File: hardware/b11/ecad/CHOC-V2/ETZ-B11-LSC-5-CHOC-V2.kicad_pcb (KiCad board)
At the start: 2 copper layers, 131.5 x 85.8 mm, 44 parts, among them SW1 Kailh_socket_PG1350, SW10 Kailh_socket_PG1350, SW11 Kailh_socket_PG1350, SW12 Kailh_socket_PG1350, SW13 Kailh_socket_PG1350, SW14 Kailh_socket_PG1350, SW15 Kailh_socket_PG1350, SW16 Kailh_socket_PG1350, SW17 Kailh_socket_PG1350, SW18 Kailh_socket_PG1350, SW19 Kailh_socket_PG1350, SW2 Kailh_socket_PG1350, SW20 Kailh_socket_PG1350, SW21 Kailh_socket_PG1350, SW22 Kailh_socket_PG1350, SW3 Kailh_socket_PG1350, SW4 Kailh_socket_PG1350, SW5 Kailh_socket_PG1350, SW6 Kailh_socket_PG1350, SW7 Kailh_socket_PG1350, SW8 Kailh_socket_PG1350, SW9 Kailh_socket_PG1350

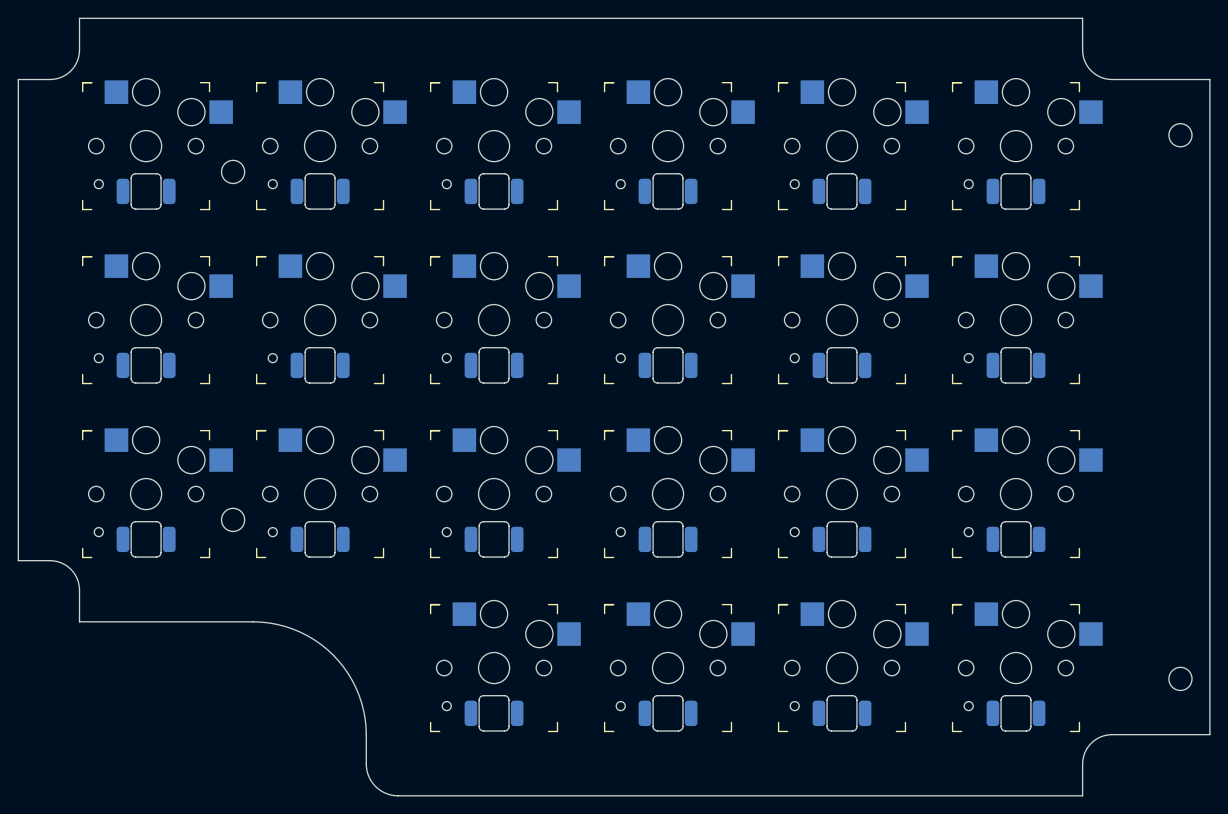
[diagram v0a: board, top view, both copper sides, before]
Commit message: refactor(hardware/b11): restructure ecad + tools, add KS-33 boards
- Rename PCB files: *-N → *-MX, *-L → *-CHOC-V2
- Reorganise ecad/ into per-family subfolders (MX/, CHOC-V2/, KS-33/)
- Add 8 blank KS-33 boards (outline only, human-populated ad-hoc)
- Apply JLCPCB-validated stackup (white/black/FR4 natural/black/white)
  to all 24 boards; SP boards at correct family thickness
- Add hardware/b11/tools/: config.py, placement.py, place-switch-sockets.py,
  place-switch-leds.py, place-display-leds.py — family-aware, non-destructive
- Archive old placement + generation scripts to hardware/scripts/_archive/
- Remove switch-origins.yaml (replaced by GRID_ORIGINS in config.py)
- Add PLAN.md tracking refactor progress

Co-Authored-By: Claude Sonnet 4.6 <noreply@anthropic.com>
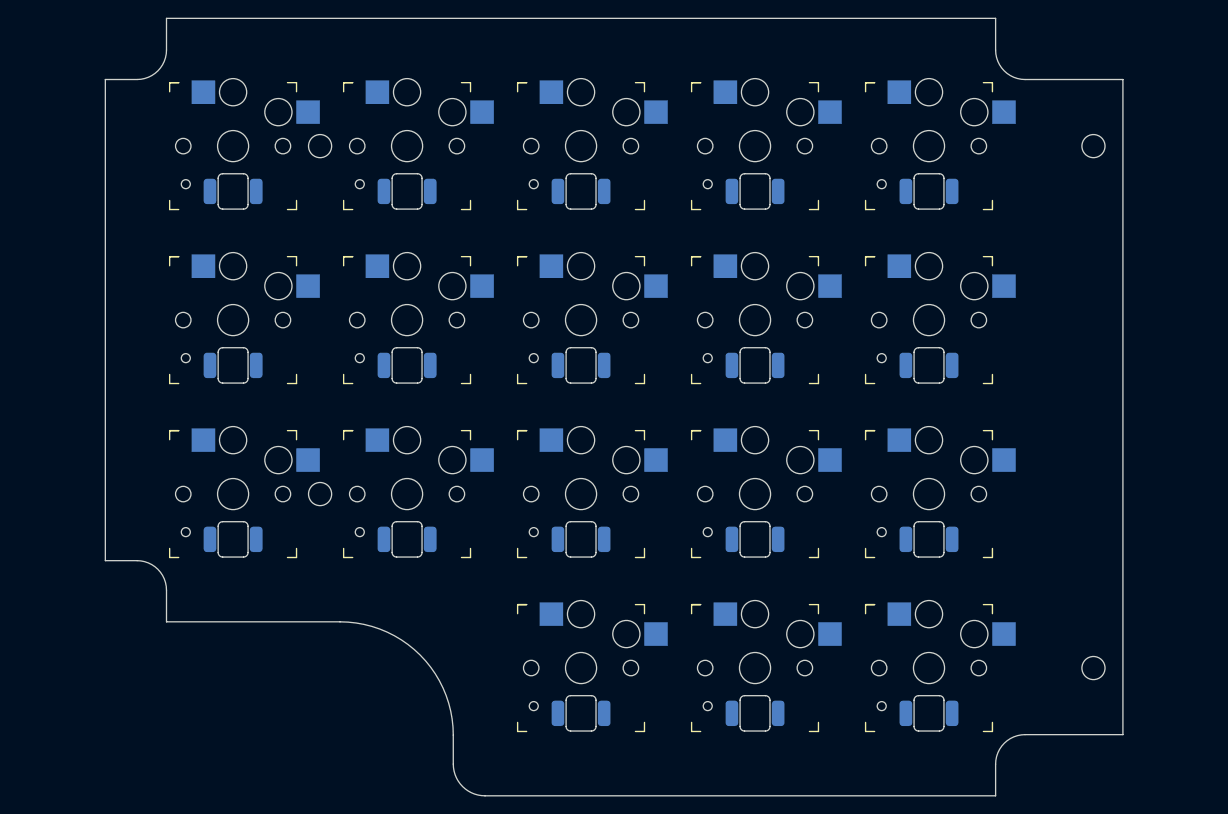
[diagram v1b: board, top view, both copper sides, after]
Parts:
- removed LED19, LED20, LED21, LED22: LED_SMD_6028_BackMount, LED_SMD_6028_BackMount
- removed SW19, SW20, SW21, SW22: Kailh_socket_PG1350, Kailh_socket_PG1350
- moved LED6 88.5 mm to (106.4, 97.5)
- moved SW6 88.5 mm to (106.4, 92.5)
- moved LED12 69.9 mm to (125.6, 116.7)
- moved SW12 69.9 mm to (125.6, 111.7)
- moved LED11 69.9 mm to (106.4, 116.7)
- moved SW11 69.9 mm to (106.4, 111.7)
- moved LED14 48.0 mm to (164.0, 116.7)
- moved SW14 48.0 mm to (164.0, 111.7)
- moved LED13 48.0 mm to (144.8, 116.7)
- moved LED15 48.0 mm to (183.2, 116.7)
- moved SW13 48.0 mm to (144.8, 111.7)
- moved SW15 48.0 mm to (183.2, 111.7)
- moved LED10 28.8 mm to (183.2, 97.5)
- moved LED9 28.8 mm to (164.0, 97.5)
- moved SW10 28.8 mm to (183.2, 92.5)
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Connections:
- SW10 pad 2: COL3 -> COL4
- SW11 pad 1: ROW1 -> ROW2
- SW11 pad 2: COL4 -> COL0
- SW12 pad 1: ROW1 -> ROW2
- SW12 pad 2: COL5 -> COL1
- SW13 pad 2: COL0 -> COL2
- SW14 pad 2: COL1 -> COL3
- SW15 pad 2: COL2 -> COL4
- SW16 pad 1: ROW2 -> ROW3
- SW16 pad 2: COL3 -> COL2
- SW17 pad 1: ROW2 -> ROW3
- SW17 pad 2: COL4 -> COL3
- SW18 pad 1: ROW2 -> ROW3
- SW18 pad 2: COL5 -> COL4
- SW6 pad 1: ROW0 -> ROW1
- SW6 pad 2: COL5 -> COL0
- SW7 pad 2: COL0 -> COL1
- SW8 pad 2: COL1 -> COL2
- SW9 pad 2: COL2 -> COL3
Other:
- board size 131.5 x 85.8 mm -> 112.3 x 85.8 mm
